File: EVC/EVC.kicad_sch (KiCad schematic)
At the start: 31 parts, among them J1 USB4105-GF-A, J2 USB4105-GF-A, U2 TCR2EF33_LMCT, U4 DRV8835DSSR, U5 DRV8835DSSR, Y1 32mhz, Y2 32mhz

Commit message: started work, prolly gonna use the ch592x since thats the next step form ch572
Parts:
- added U6: CH592X, QFN32_4X4, symbol CHXXX:CH592X (Altium Display 2)
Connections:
- net GND: now also U4.13 (PAD), U4.6 (GND), U5.13 (PAD), U5.6 (GND)
- net APH: now reaches U5.10 (AIN1/APHASE)
- net APH: now also U3.20 (PA2/R/T1/SDA2/SCS_/PWM2/TMR1/CN)
- net at U5.11 (MODE): now also C9.1, U5.12 (VCC)
- net AOUT1: now reaches U5.2 (AOUT1)
- net AOUT2: now reaches U5.3 (AOUT2)
- net BOUT1: now reaches U5.4 (BOUT1)
- net BOUT2: now reaches U5.5 (BOUT2)
- net BEN: now reaches U5.7 (BIN2/BENBL)
- net BEN: now also U3.16 (PA7/MOSI/T4/PWM1/TMR/RST_/CP1)
- net BPH: now reaches U5.8 (BIN1/BPHASE)
- net BPH: now also U3.17 (PA10/R6/T7)
- net AEN: now reaches U5.9 (AIN2/AENBL)
- net AEN: now also U3.18 (PA11/R7/T6)
- net APH-1: now reaches U4.10 (AIN1/APHASE)
- net at U4.11 (MODE): now also C14.1, U4.12 (VCC)
- net AOUT1-1: now reaches U4.2 (AOUT1)
- net AOUT2-2: now reaches U4.3 (AOUT2)
- net BOUT1-1: now reaches U4.4 (BOUT1)
- net BOUT2-2: now reaches U4.5 (BOUT2)
- net BEN-1: now reaches U4.7 (BIN2/BENBL)
- net BPH-1: now reaches U4.8 (BIN1/BPHASE)
- net AEN-1: now reaches U4.9 (AIN2/AENBL)
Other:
- moved on the sheet: C10, C11, C12, C13, C14, C6, C7, C8, C9, J2, R4, R5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

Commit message: started work on layout, design nearly done, need to order components soon...
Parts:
- removed C1, C2, C6, C7: 2.2uF, Footprint:0603, symbol 0603:C_0603
- removed C3, C8: 0.1uF, Footprint:0603, symbol 0603:C_0603
- removed J2: USB4105-GF-A, Footprint:usbc, symbol usbc:USB4105-GF-A
- removed R3, R4: 1.5k, Footprint:0603, symbol 0603:R_0603
- removed R5, R6: 5.1k, Footprint:0603, symbol fab:R_0603
- removed S1: TL3365AF180QG, Footprint:button, symbol button:TL3365AF180QG
- removed U1, U3: ~, Footprint:CH572D, symbol CH572D:CH572D
- removed U6: CH592X, QFN32_4X4, symbol CHXXX:CH592X (Altium Display 2)
- removed Y2: 32mhz, Footprint:32mhz crystal, symbol 32mhz crystal:XRCGB32M000F2P01R0
- added C1: 2.2uf, Footprint:C_0603, symbol fab:C_0603
- added C2: 0.1uf, Footprint:C_0603, symbol fab:C_0603
- added C3: .47uf, Footprint:C_0603, symbol fab:C_0603
- added C6: 4.7uF, Footprint:C_0603, symbol fab:C_0603
- added C7: 0.5pf, Footprint:C_0603, symbol fab:C_0603
- added C8: 1.5pf, Footprint:C_0603, symbol fab:C_0603
- added CN1, CN2, CN3, CN4: HC-ZH1.5-6AW, EasyEDA:CONN-TH_6P-P1.50_HCTL_C-ZH1.5-6AW, symbol EasyEDA:HC-ZH1.5-6AW
- added L1: 10uH, Footprint:0603, symbol 0603:L_0603
- added L2: 3.9nh, Footprint:0603, symbol 0603:L_0603
- added U1: CH592X, CHXXX:QFN32_4X4, symbol CHXXX_2:CH592X
- added U3: C30732.768NCXE20, EasyEDA:HC-49S_L7.2-W3.2, symbol EasyEDA:C30732.768NCXE20
- added U6: ANT3216LL00R2400A, EasyEDA:ANT-SMD_L3.2-W1.6, symbol EasyEDA:ANT3216LL00R2400A
- C10, C13, C14, C9: footprint fab:C_0603 -> Footprint:C_0603
- C11: footprint fab:C_1206 -> Footprint:C_1206
- C12: value C_1206 -> 22uf; footprint fab:C_1206 -> Footprint:C_1206
- C4, C5: footprint Footprint:0603 -> Footprint:C_0603
- Y1: value 32mhz -> XRCGB32M000F2P01R0
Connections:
- net +3.3V is gone; now on net PWR_GND: S2.1, S2.2
- net D+-1 is gone; now on net D+: J1.A6 (DP1), J1.B6 (DP2)
- net D--1 is gone; now on net D-: J1.A7 (DN1), J1.B7 (DN2)
- net AEN: now also U5.8 (BIN1/BPHASE), U1.8 (PA7/TXD2_/PWM5_/DCD/AIN11); no longer U5.9 (AIN2/AENBL)
- net AEN-1: now also U1.30 (PA13/SCK0/PWM5/AIN3)
- net APH: now also U5.7 (BIN2/BENBL), U1.10 (PA9/TMR0/TXD1/AIN13); no longer U5.10 (AIN1/APHASE)
- net APH-1: now also U1.28 (PA15/MISO/RXD0_/AIN5)
- net BEN: now also U5.10 (AIN1/APHASE), U1.7 (PA6/PWM4_/RXD2_/RI/AIN10); no longer U5.7 (BIN2/BENBL)
- net BEN-1: now also U1.31 (PA12/SCS/PWM4/AIN2)
- net BPH: now also U5.9 (AIN2/AENBL), U1.9 (PA8/RXD1/AIN12); no longer U5.8 (BIN1/BPHASE)
- net BPH-1: now also U1.29 (PA14/MOSI/TXD0_/AIN4)
- net D+: now also U1.15 (PB11/UD+/TMR2_)
- net D-: now also U1.16 (PB10/UD-/TMR1_)
- net PWR_3V3: now also C1.1, CN4.2, U1.6 (VIO33/VDD33)
- net PWR_GND: now also U4.13 (PAD), U4.6 (GND), U5.13 (PAD), C1.2, C2.1, C3.1, C6.2, C7.2, C8.2, CN4.5, U1.0 (GND)
- net BOOT: now reaches S2.3, S2.4
- net BOOT: now also U1.20 (PB22/TMR3/RXD2)
- net XO: now reaches Y1.3
- net XO: now also U1.22 (X32MI)
- net XI: now reaches Y1.1
- net XI: now also U1.21 (X32MO)
- net AOUT1 renamed 1OUT1
- net 1OUT1: now also CN4.6
- net AOUT1-1 renamed 3OUT1
- net AOUT2 renamed 1OUT2
- net 1OUT2: now also CN4.1
- net AOUT2-2 renamed 3OUT2
- net BOUT1 renamed 2OUT1
- net BOUT1-1 renamed 4OUT1
- net BOUT2 renamed 2OUT2
- net BOUT2-2 renamed 4OUT2
- removed net GND: U4.13 (PAD), U4.6 (GND), U5.13 (PAD), U5.6 (GND)
- new net: C8.1, L2.1, U6.1
- new net 1ENC1: CN4.3, U1.11 (PB15/TCK/MISO_/SCL/DTR)
- new net 1ENC2: CN4.4, U1.12 (PB14/TIO/MOSI_/SDA/PWM10/DSR)
- new net 2ENC1: U1.13 (PB13/SCK0_/TXD1_/DCD_)
- new net 2ENC2: U1.14 (PB12/SCS_/RXD1_/RI_)
- new net 3ENC1: U1.26 (PA4/RXD3/AIN0)
- new net 3ENC2: U1.27 (PA5/TXD3/AIN1)
- new net 4ENC1: U1.2 (PB6/RTS/PWM8/AIN9)
- new net 4ENC2: U1.3 (PB0/PWM6/CTS/AIN8)
- new net ANT: C7.1, L2.2, U1.24 (ANT)
- new net VDCIA: C2.2, C6.1, L1.2, U1.25 (VDCIA), U1.4 (VDCID)
- new net VINTA: C3.2, U1.23 (VINTA)
- new net VSW: L1.1, U1.5 (VSW)
- new net XI_32khz: U1.1 (PA10/X32KI/TMR1), U3.1
- new net XO_32khz: U1.32 (PA11/X32KO/TMR2), U3.2
- no-connect marks 8 -> 2
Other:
- note removed: "Boot/Download button"
- moved on the sheet: C10, C11, C12, C13, C14, C9, U4, U5

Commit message: done
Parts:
- removed C4: 0.1uF, Footprint:C_0603, symbol fab:C_0603
- removed C5: 1uF, Footprint:C_0603, symbol fab:C_0603
- removed C7: 0.5pf, Footprint:C_0603, symbol fab:C_0603
- removed C8: 1.5pf, Footprint:C_0603, symbol fab:C_0603
- removed L2: 3.9nh, Footprint:0603, symbol 0603:L_0603
- removed U2: TCR2EF33_LMCT, Footprint:voltage regulator, symbol voltage regulator:TCR2EF33_LMCT
- removed U3: C30732.768NCXE20, EasyEDA:HC-49S_L7.2-W3.2, symbol EasyEDA:C30732.768NCXE20
- removed U6: ANT3216LL00R2400A, EasyEDA:ANT-SMD_L3.2-W1.6, symbol EasyEDA:ANT3216LL00R2400A
- added C15, C16: 0.1uF, Footprint:C_0603, symbol fab:C_0603
- added C17, C18: 10uf, Footprint:C_0603, symbol fab:C_0603
- added J2: screen, Footprint:PinHeader_01x04_P2.54mm_Vertical_THT_D1mm, symbol fab:PinHeader_01x04_P2.54mm_Vertical_THT_D1mm
- added P1: WJ500V-5.08-2P-14-00A, EasyEDA:CONN-TH_2P-P5.00_WJ500V-5.08-2P, symbol EasyEDA:WJ500V-5.08-2P-14-00A
- added Q1: AMS1117-3.3V_C5120796, EasyEDA:SOT-89-3_L4.5-W2.5-P1.50-LS4.2-BR, symbol EasyEDA:AMS1117-3.3V_C5120796
- added S1, S3: TL3365AF180QG, Footprint:button, symbol button:TL3365AF180QG
- added X1: Q13FC1350000400, EasyEDA:FC-135R_L3.2-W1.5, symbol EasyEDA:Q13FC1350000400
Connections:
- net PWR_3V3 is gone; now on net VDD33: C1.1, CN4.2, U1.6 (VIO33/VDD33)
- net 1OUT1: now also CN4.1; no longer CN4.6
- net 1OUT2: now also CN4.6; no longer CN4.1
- net 2ENC1: now also CN2.3
- net 2ENC2: now also CN2.4
- net 2OUT1: now also CN2.1
- net 2OUT2: now also CN2.6
- net 3ENC1: now also CN1.3, U1.27 (PA5/TXD3/AIN1); no longer U1.26 (PA4/RXD3/AIN0)
- net 3ENC2: now also CN1.4, U1.26 (PA4/RXD3/AIN0); no longer U1.27 (PA5/TXD3/AIN1)
- net 3OUT1: now also CN1.6
- net 3OUT2: now also CN1.1
- net 4ENC1: now also CN3.3
- net 4ENC2: now also CN3.4
- net 4OUT1: now also CN3.1
- net 4OUT2: now also CN3.6
- net APH: now also U1.9 (PA8/RXD1/AIN12); no longer U1.10 (PA9/TMR0/TXD1/AIN13)
- net BPH: now also U1.10 (PA9/TMR0/TXD1/AIN13); no longer U1.9 (PA8/RXD1/AIN12)
- net PWR_5V: now also C10.2, C11.2, C12.2, C13.2, U4.1 (VM), U5.1 (VM), C16.2, C18.2, P1.1, Q1.3 (VIN)
- net PWR_GND: now also CN1.5, CN2.5, CN3.5, C15.1, C16.1, C17.1, C18.1, J2.1 (Pin_1), P1.2, Q1.1 (ADJ/GND), S1.1, S1.2, S3.1, S3.2
- net XI_32khz: now also X1.1
- net XO_32khz: now also X1.2
- net VDD33: now reaches C9.1, U5.11 (MODE), U5.12 (VCC)
- net VDD33: now also C14.1, CN1.2, CN2.2, CN3.2, U4.11 (MODE), U4.12 (VCC), C15.2, C17.2, J2.2 (Pin_2), Q1.2 (VOUT)
- net SCL/CT10: now reaches U1.17 (PB7/TXD0/PWM9)
- net SCL/CT10: now also J2.3 (Pin_3), S3.3, S3.4
- net SDA/CT1: now reaches U1.18 (PB4/RXD0/PWM7)
- net SDA/CT1: now also J2.4 (Pin_4), S1.3, S1.4
- net ANT: no longer names the net of U1.24 (ANT)
- no-connect marks 2 -> 4
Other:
- moved on the sheet: CN1, CN2, CN3, CN4

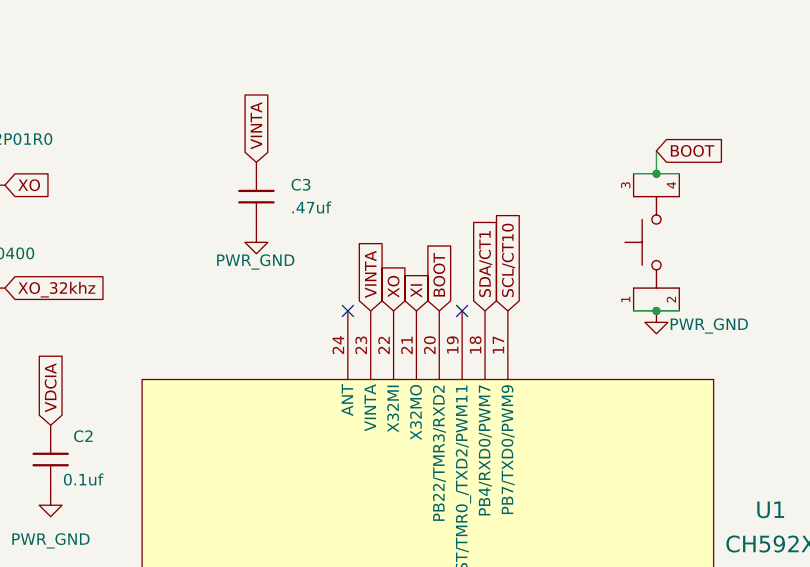
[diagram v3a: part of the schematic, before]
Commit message: fixed that one connector + flipped screw terminal
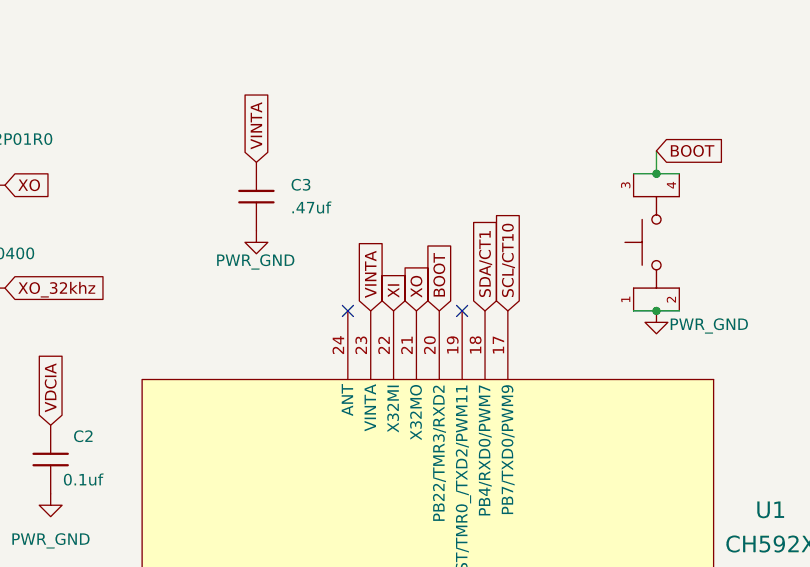
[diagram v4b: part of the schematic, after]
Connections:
- net XI: now also U1.22 (X32MI); no longer U1.21 (X32MO)
- net XO: now also U1.21 (X32MO); no longer U1.22 (X32MI)

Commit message: fixed some stuff reorder should be aokay
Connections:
- net AEN: now also U5.9 (AIN2/AENBL); no longer U5.8 (BIN1/BPHASE)
- net APH: now also U5.10 (AIN1/APHASE); no longer U5.7 (BIN2/BENBL)
- net BEN: now also U5.7 (BIN2/BENBL); no longer U5.10 (AIN1/APHASE)
- net BPH: now also U5.8 (BIN1/BPHASE); no longer U5.9 (AIN2/AENBL)
- net PWR_GND: now also U5.6 (GND)
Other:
- moved on the sheet: CN4
